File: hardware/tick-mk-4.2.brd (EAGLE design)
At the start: 96 x 53 mm, 28 parts, among them IC1 ATMEGA328P, IC2 DS1338, IC3 LM1117, Y1 16MHz

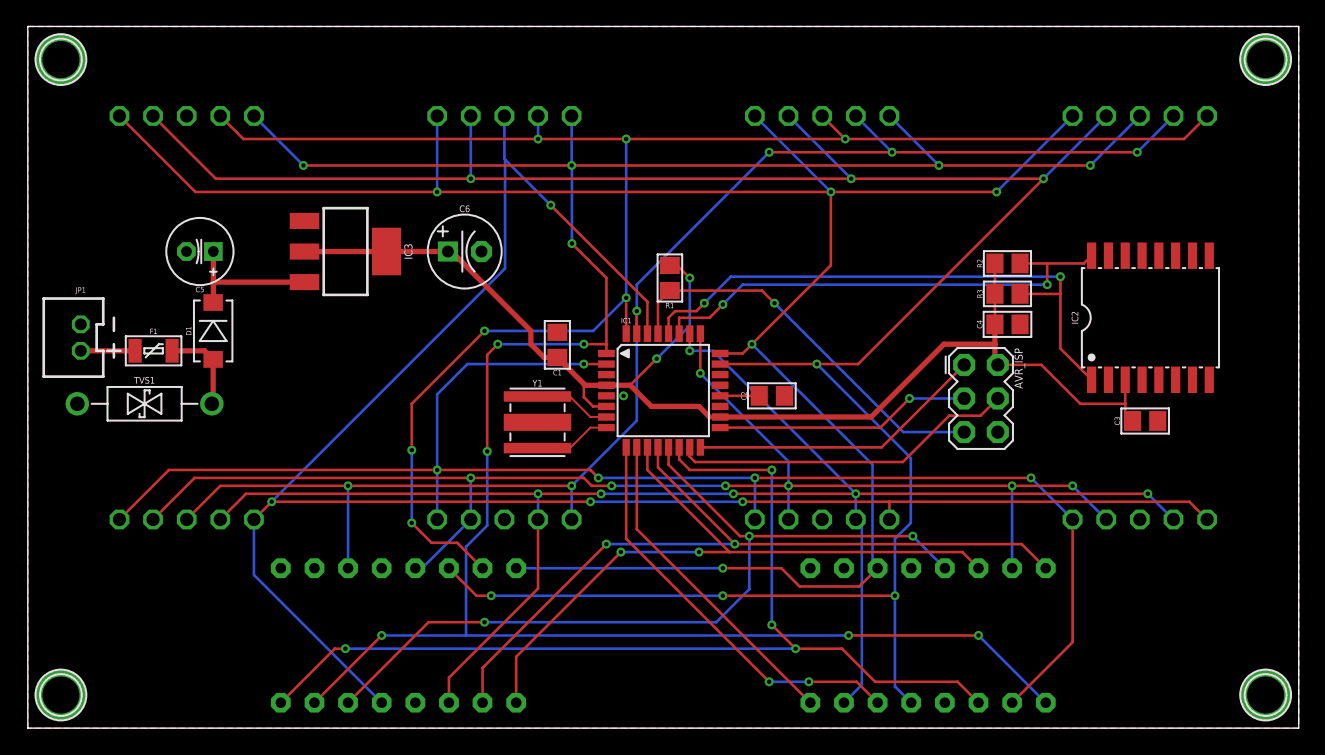
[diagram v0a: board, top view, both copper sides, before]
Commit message: swapping most SMD components to PTH ones except for the ICs
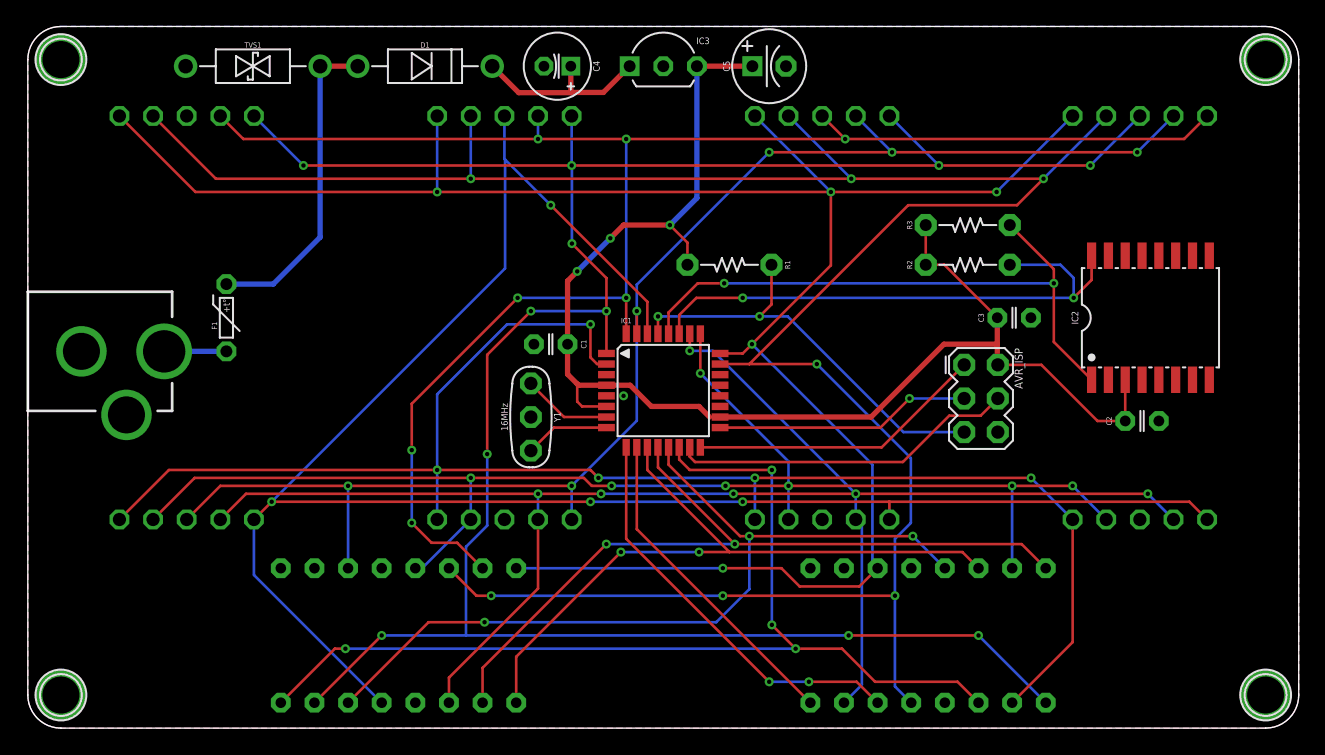
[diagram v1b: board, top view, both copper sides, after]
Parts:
- removed C6: 100uF, A_butts:E2,5-6
- removed JP1: M02JST-PTH-VERT, A_butts:JST-2-PH-VERT-PTH
- added PWR: DCBARRELPTH, A_butts:DCJACK_2MM_PTH
- C1, C2: device A_butts:C0805 -> A_butts:C025-024X044
- C3: value 0.1uF -> 1uF; device A_butts:C0805 -> A_butts:C025-024X044
- C4: value 1uF -> 10uF; device A_butts:C0805 -> A_butts:E2-5
- C5: value 10uF -> 100uF; device A_butts:E2-5 -> A_butts:E2,5-6
- D1: value 1N4001 -> 1N5819; device A_butts:SMA-DIODE -> A_butts:DIODE-10.16MM
- F1: device A_butts:PTC-1206 -> A_butts:PTC-PTH-5.08MM
- IC3: value LM1117 -> LM2941; device A_butts:SOT223 -> A_butts:TO-92-AMMO
- R1, R2, R3: device A_butts:R0805 -> A_butts:RESISTOR-AXIAL-PTH-6.35MM
- Y1: device A_butts:RESONATOR-4.7X4.1X1.2MM -> A_butts:RESONATOR-PTH
- moved C5 45.2 mm to (56.0, 50.0), turned to 0 degrees
- moved C4 39.2 mm to (40.0, 50.0), turned to 180 degrees
- moved C2 28.0 mm to (84.2, 23.2)
- moved IC3 27.8 mm to (48.0, 50.0), turned to 0 degrees
- moved TVS1 26.8 mm to (17.0, 50.0)
- moved D1 25.6 mm to (30.0, 50.0), turned to 0 degrees
- moved C3 12.6 mm to (74.5, 31.0)
- moved F1 6.04 mm to (15.0, 31.0), turned to 90 degrees
- moved R3 6.00 mm to (71.0, 38.0)
- moved R1 4.61 mm to (53.0, 35.0), turned to 180 degrees
- moved R2 3.00 mm to (71.0, 35.0)
- moved Y1 0.64 mm to (38.0, 23.5)
- moved C1 0.50 mm to (39.5, 29.0), turned to 180 degrees
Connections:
- removed net N$1: C2.1, IC1.20
- net GND: now also C4.-, IC3.2, PWR.GND; no longer C4.2, C6.-, IC3.1, JP1.2
- net N$4: now also F1.P$2; no longer F1.2
- net N$7: now also F1.P$1, PWR.PWR; no longer F1.1, JP1.1
- net N$8: now also C4.+, IC3.1; no longer C5.+, IC3.3
- net RST: now also R1.P$1; no longer R1.1
- net SCL: now also R3.P$2; no longer R3.2
- net SDA: now also R2.P$2; no longer R2.2
- net VCC: now also C2.1, C5.+, IC3.3, R1.P$2, R2.P$1, R3.P$1; no longer C4.1, C6.+, IC3.2, IC3.4, R1.2, R2.1, R3.1
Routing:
- net N$4: track 6.76 -> 24.3 mm
- net VCC: track 97.0 -> 105.0 mm, vias 2 -> 3
- net A0: track 181.7 -> 186.8 mm
- net SDA: track 37.3 -> 42.2 mm
- net D4: track 117.2 -> 121.1 mm
- net N$8: track 10.7 -> 14.0 mm
- net N$1: track 2.96 -> 0.00 mm
- net RST: track 30.3 -> 32.3 mm, vias 1 -> 2
- net SCL: track 43.9 -> 45.9 mm
- net D3: track 185.0 -> 186.0 mm
- net N$2: track 5.85 -> 6.78 mm
- net N$7: track 4.10 -> 4.70 mm
- net N$3: track 5.85 -> 6.43 mm
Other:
- outline, holes or cut-outs redrawn

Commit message: layout complete for rev 4.2
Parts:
- added BAT1: 20mm coincell, A_butts:BATTCON_20MM_MINE
- added U$1, U$2: (no value), A_butts:CC-BY-SA-4.0-NO-URL
- added U$3: (no value), A_butts:COW
- added U$4: (no value), A_butts:COW_SMALL
- added U$5: (no value), A_butts:OSHWLOGO_TOP_0.2
- DIGIT1, DIGIT2, DIGIT3, DIGIT4: value 7SEG_1DIGPTH-25.4MM -> 7SEG_1DIGPTH-25.4MM-BARE; device A_butts:7SEG_1DIG_25.4MM -> A_butts:7SEG_1DIG_25.4MM_NOSILK
- IC3: value LM2941 -> L7805; device A_butts:TO-92-AMMO -> A_butts:TO220-IGO-THERMPAD
- PWR: value DCBARRELPTH -> M02JST-PTH-VERT; device A_butts:DCJACK_2MM_PTH -> A_butts:JST-2-PH-VERT-PTH
- moved IC3 34.6 mm to (17.1, 34.5), turned to 90 degrees
- moved D1 30.8 mm to (9.50, 27.0)
- moved C4 29.2 mm to (22.0, 27.0), turned to 0 degrees
- moved TVS1 28.0 mm to (9.50, 23.0), turned to 180 degrees
- moved C5 26.4 mm to (33.0, 37.0)
- moved C2 22.6 mm to (62.0, 27.5), turned to 90 degrees
- moved PWR 20.9 mm to (4.42, 9.00), turned to 90 degrees
- moved R2 18.1 mm to (53.0, 36.5)
- moved R3 18.0 mm to (53.0, 39.0)
- moved F1 16.8 mm to (4.42, 18.0)
- moved IC2 15.5 mm to (69.4, 32.4)
- moved C3 15.4 mm to (59.5, 27.5), turned to 90 degrees
- moved AVR_ISP 2.86 mm to (70.8, 22.3), turned to 0 degrees
- moved C1 1.84 mm to (39.0, 27.2)
- moved R1 1.00 mm to (53.0, 34.0)
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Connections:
- new net N$1: BAT1.TOP@1, BAT1.TOP@2, IC2.14
- net GND: now also BAT1.BOTTOM, IC3.4, IC3.GND, PWR.1; no longer IC3.2, PWR.GND
- net N$7: now also PWR.2; no longer PWR.PWR
- net N$8: now also IC3.IN; no longer IC3.1
- net VCC: now also IC3.OUT; no longer IC3.3
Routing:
- net GND: track 0.00 -> 46.3 mm, vias 1 -> 2
- net N$1: track 0.00 -> 45.2 mm, vias 0 -> 2
- net N$4: track 24.3 -> 6.46 mm
- net SCL: track 45.9 -> 31.6 mm
- net VCC: track 105.0 -> 91.4 mm, vias 3 -> 0
- net SDA: track 42.2 -> 29.4 mm
- net D2: track 130.2 -> 138.1 mm
- net D4: track 121.1 -> 128.9 mm, vias 5 -> 6
- net RST: track 32.3 -> 37.7 mm
- net D1: track 107.5 -> 112.6 mm
- net D12/MISO: track 22.5 -> 17.5 mm
- net N$3: track 6.43 -> 10.2 mm
- net D11/MOSI: track 26.1 -> 22.5 mm
- net D9: track 63.3 -> 59.8 mm
- net D3: track 186.0 -> 189.2 mm
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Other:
- board text added: "Terribly Illuminated Chronology Keeper v4.2"
